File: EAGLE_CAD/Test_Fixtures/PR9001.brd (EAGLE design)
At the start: 62.5 x 47.5 mm, 14 parts, among them T10 PR9001_TESTPOINT, T11 PR9001_TESTPOINT, T12 PR9001_TESTPOINT, T13 PR9001_TESTPOINT, T2 PR9001_TESTPOINT, T3 PR9001_TESTPOINT, T4 PR9001_TESTPOINT, T5 PR9001_TESTPOINT

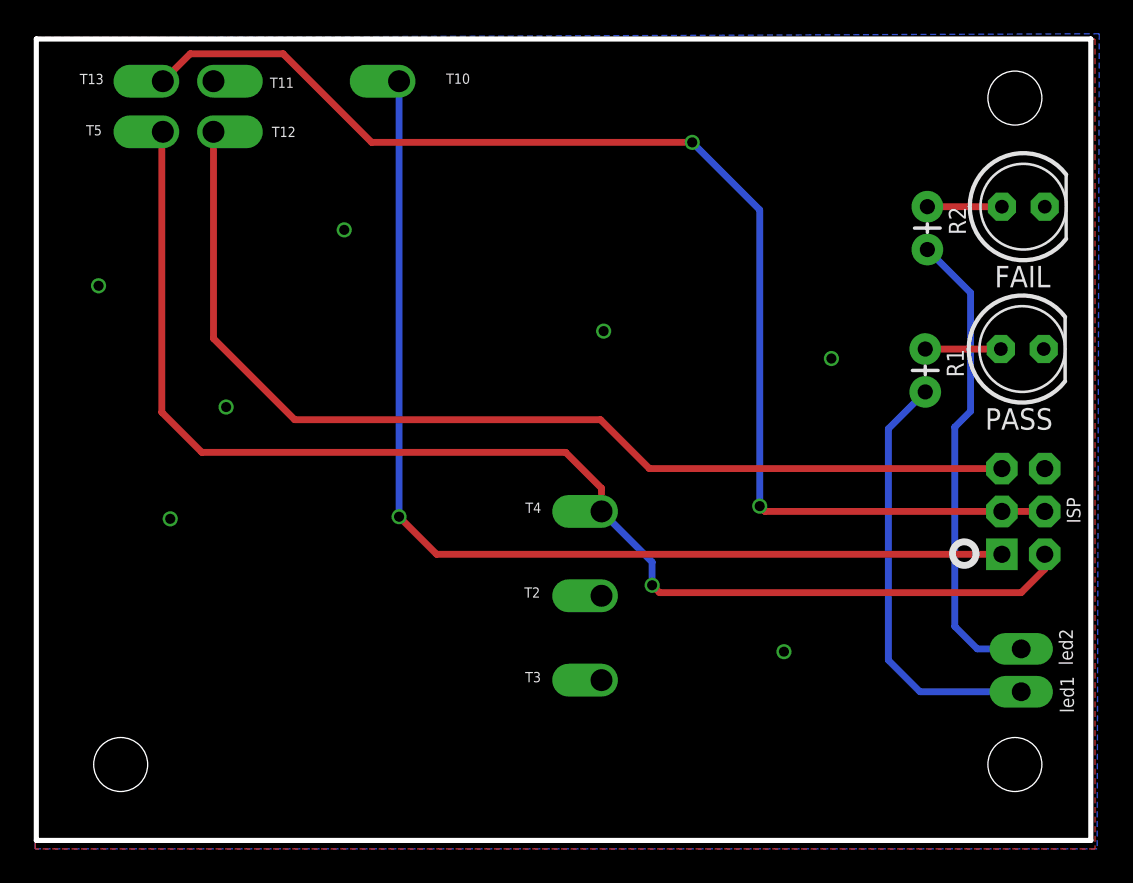
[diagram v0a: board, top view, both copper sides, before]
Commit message: PR9001 Programming Fixture
Updated layout and added an additional mounting hole.
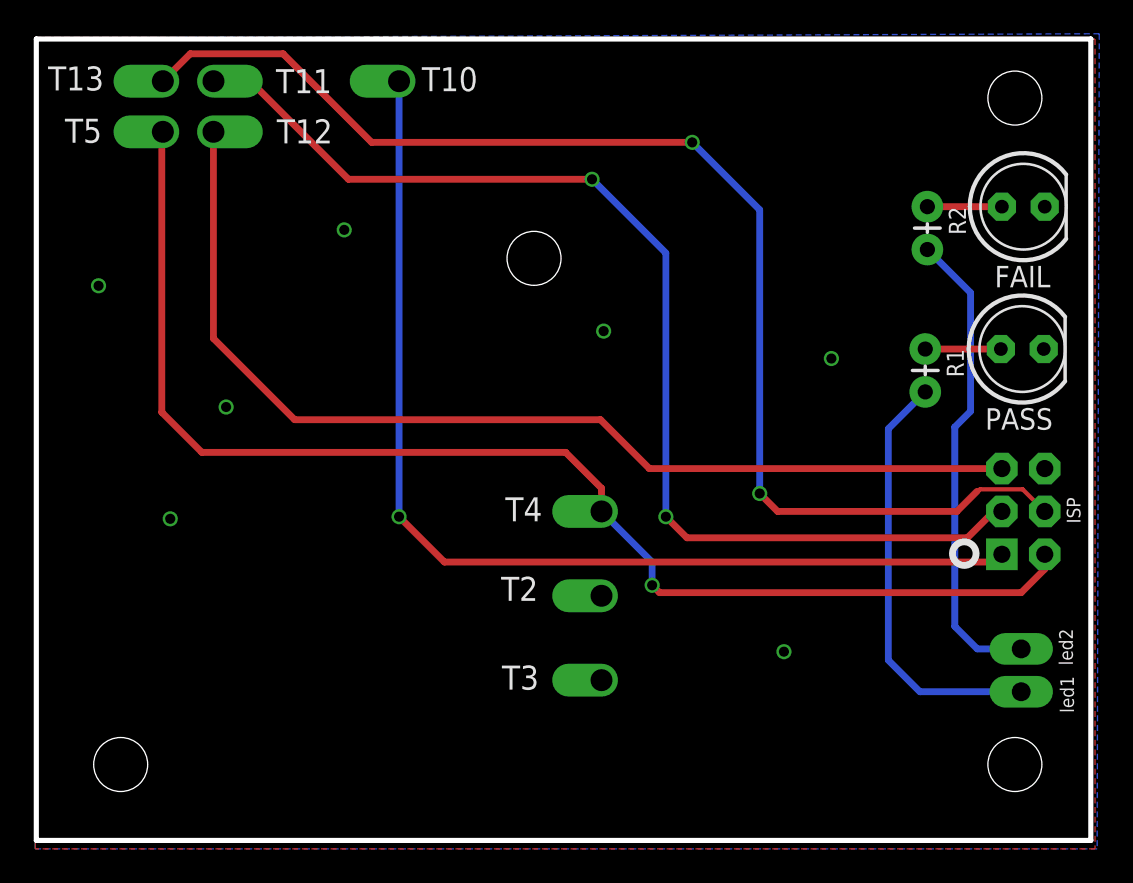
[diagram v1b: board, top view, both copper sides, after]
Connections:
- net SCLK: now also ISP.3
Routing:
- net SCLK: track 0.00 -> 67.7 mm, vias 0 -> 2
- net SDIO: track 74.5 -> 75.1 mm
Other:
- board text added: "PR9001 Fixture For Use With PR9024"
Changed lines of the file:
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@@
 <text x="87" y="28.0625" size="0.8128" layer="25" rot="R90">led1</text>
 <text x="86.9375" y="30.875" size="0.8128" layer="25" rot="R90">led2</text>
+<hole x="55" y="55" drill="3.2"/>
+<text x="61.6875" y="46.25" size="1.4224" layer="26" rot="MR0">PR9001 Fixture
+For Use With PR9024 </text>
 </plain>
 <attributes>
@@
 </element>
 <element name="T2" library="PR_Parts_Library" package="PR9001_TESTPOINT" value="PR9001_TESTPOINT" x="59" y="35" locked="yes" smashed="yes" rot="MR0">
-<attribute name="NAME" x="54.425" y="34.8876" size="0.6096" layer="25" font="vector" ratio="16"/>
+<attribute name="NAME" x="53.05" y="34.7001" size="1.4224" layer="25" font="vector" ratio="16"/>
 <attribute name="VALUE" x="59.508" y="34.238" size="0.254" layer="28" rot="MR0"/>
 </element>
 <element name="T3" library="PR_Parts_Library" package="PR9001_TESTPOINT" value="PR9001_TESTPOINT" x="59" y="30" locked="yes" smashed="yes" rot="MR0">
-<attribute name="NAME" x="54.475" y="29.8751" size="0.6096" layer="25" font="vector" ratio="16"/>
+<attribute name="NAME" x="53.1" y="29.4376" size="1.4224" layer="25" font="vector" ratio="16"/>
 <attribute name="VALUE" x="59.508" y="29.238" size="0.254" layer="28" rot="MR0"/>
 </element>
 <element name="T4" library="PR_Parts_Library" package="PR9001_TESTPOINT" value="PR9001_TESTPOINT" x="59" y="40" locked="yes" smashed="yes" rot="MR0">
-<attribute name="NAME" x="54.4875" y="39.9126" size="0.6096" layer="25" font="vector" ratio="16"/>
+<attribute name="NAME" x="53.3" y="39.4126" size="1.4224" layer="25" font="vector" ratio="16"/>
 <attribute name="VALUE" x="59.508" y="39.238" size="0.254" layer="28" rot="MR0"/>
 </element>
 <element name="T5" library="PR_Parts_Library" package="PR9001_TESTPOINT" value="PR9001_TESTPOINT" x="33" y="62.5" locked="yes" smashed="yes" rot="MR0">
-<attribute name="NAME" x="28.45" y="62.2876" size="0.6096" layer="25" font="vector" ratio="16"/>
+<attribute name="NAME" x="27.2" y="61.8501" size="1.4224" layer="25" font="vector" ratio="16"/>
 <attribute name="VALUE" x="33.508" y="61.738" size="0.254" layer="28" rot="MR0"/>
 </element>
 <element name="T10" library="PR_Parts_Library" package="PR9001_TESTPOINT" value="PR9001_TESTPOINT" x="47" y="65.5" locked="yes" smashed="yes" rot="MR0">
-<attribute name="NAME" x="49.79" y="65.3451" size="0.6096" layer="25" font="vector" ratio="16"/>
+<attribute name="NAME" x="48.3525" y="64.9076" size="1.4224" layer="25" font="vector" ratio="16"/>
 <attribute name="VALUE" x="47.508" y="64.738" size="0.254" layer="28" rot="MR0"/>
 </element>
 <element name="T11" library="PR_Parts_Library" package="PR9001_TESTPOINT" value="PR9001_TESTPOINT" x="36" y="65.5" locked="yes" smashed="yes" rot="MR180">
-<attribute name="NAME" x="40.7625" y="65.7124" size="0.6096" layer="25" font="vector" ratio="16" rot="R180"/>
+<attribute name="NAME" x="43.0125" y="66.2124" size="1.4224" layer="25" font="vector" ratio="16" rot="R180"/>
 <attribute name="VALUE" x="35.492" y="66.262" size="0.254" layer="28" rot="MR180"/>
 </element>
 <element name="T12" library="PR_Parts_Library" package="PR9001_TESTPOINT" value="PR9001_TESTPOINT" x="36" y="62.5" locked="yes" smashed="yes" rot="MR180">
-<attribute name="NAME" x="40.875" y="62.7999" size="0.6096" layer="25" font="vector" ratio="16" rot="R180"/>
+<attribute name="NAME" x="43.0625" y="63.2374" size="1.4224" layer="25" font="vector" ratio="16" rot="R180"/>
 <attribute name="VALUE" x="35.492" y="63.262" size="0.254" layer="28" rot="MR180"/>
 </element>
 <element name="T13" library="PR_Parts_Library" package="PR9001_TESTPOINT" value="PR9001_TESTPOINT" x="33" y="65.5" locked="yes" smashed="yes" rot="MR0">
-<attribute name="NAME" x="28.075" y="65.3251" size="0.6096" layer="25" font="vector" ratio="16"/>
+<attribute name="NAME" x="26.2" y="64.9501" size="1.4224" layer="25" font="vector" ratio="16"/>
 <attribute name="VALUE" x="33.508" y="64.738" size="0.254" layer="28" rot="MR0"/>
 </element>
@@
 <contactref element="ISP" pad="1"/>
 <contactref element="T10" pad="P$1"/>
-<wire x1="82.73" y1="37.46" x2="49.2275" y2="37.46" width="0.4064" layer="1"/>
-<wire x1="49.2275" y1="37.46" x2="47" y2="39.6875" width="0.4064" layer="1"/>
+<wire x1="49.6875" y1="37" x2="47" y2="39.6875" width="0.4064" layer="1"/>
 <via x="47" y="39.6875" extent="1-16" drill="0.6"/>
 <wire x1="47" y1="39.6875" x2="47" y2="65.5" width="0.4064" layer="16"/>
+<wire x1="49.6875" y1="37" x2="82.27" y2="37" width="0.4064" layer="1"/>
+<wire x1="82.27" y1="37" x2="82.73" y2="37.46" width="0.4064" layer="1"/>
 </signal>
 <signal name="SCLK">
 <contactref element="T11" pad="P$1"/>
+<contactref element="ISP" pad="3"/>
+<wire x1="82.73" y1="40" x2="82.25" y2="40" width="0.4064" layer="1"/>
+<wire x1="82.25" y1="40" x2="80.6875" y2="38.4375" width="0.4064" layer="1"/>
+<wire x1="80.6875" y1="38.4375" x2="64.0625" y2="38.4375" width="0.4064" layer="1"/>
+<via x="58.4375" y="59.6875" extent="1-16" drill="0.6"/>
+<wire x1="58.4375" y1="59.6875" x2="44" y2="59.6875" width="0.4064" layer="1"/>
+<wire x1="44" y1="59.6875" x2="38.1875" y2="65.5" width="0.4064" layer="1"/>
+<wire x1="38.1875" y1="65.5" x2="36" y2="65.5" width="0.4064" layer="1"/>
+<wire x1="64.0625" y1="38.4375" x2="62.8125" y2="39.6875" width="0.4064" layer="1"/>
+<via x="62.8125" y="39.6875" extent="1-16" drill="0.6"/>
+<wire x1="62.8125" y1="39.6875" x2="62.8125" y2="55.3125" width="0.4064" layer="16"/>
+<wire x1="62.8125" y1="55.3125" x2="58.4375" y2="59.6875" width="0.4064" layer="16"/>
 </signal>
 <signal name="SDIO">
 <contactref element="ISP" pad="4"/>
 <contactref element="T13" pad="P$1"/>
-<wire x1="85.27" y1="40" x2="68.6875" y2="40" width="0.4064" layer="1"/>
-<wire x1="68.6875" y1="40" x2="68.375" y2="40.3125" width="0.4064" layer="1"/>
-<via x="68.375" y="40.3125" extent="1-16" drill="0.6"/>
-<wire x1="68.375" y1="40.3125" x2="68.375" y2="57.875" width="0.4064" layer="16"/>
 <wire x1="68.375" y1="57.875" x2="64.375" y2="61.875" width="0.4064" layer="16"/>
 <via x="64.375" y="61.875" extent="1-16" drill="0.6"/>
@@
 <wire x1="40.125" y1="67.125" x2="34.625" y2="67.125" width="0.4064" layer="1"/>
 <wire x1="34.625" y1="67.125" x2="33" y2="65.5" width="0.4064" layer="1"/>
+<wire x1="80.0625" y1="40" x2="81.25" y2="41.1875" width="0.4064" layer="1"/>
+<wire x1="81.25" y1="41.1875" x2="81.3125" y2="41.1875" width="0.254" layer="1"/>
+<wire x1="81.3125" y1="41.1875" x2="81.4375" y2="41.3125" width="0.254" layer="1"/>
+<wire x1="81.4375" y1="41.3125" x2="83.9575" y2="41.3125" width="0.254" layer="1"/>
+<wire x1="83.9575" y1="41.3125" x2="85.27" y2="40" width="0.254" layer="1"/>
+<wire x1="80.0625" y1="40" x2="69.4375" y2="40" width="0.4064" layer="1"/>
+<wire x1="69.4375" y1="40" x2="68.375" y2="41.0625" width="0.4064" layer="1"/>
+<via x="68.375" y="41.0625" extent="1-16" drill="0.6"/>
+<wire x1="68.375" y1="41.0625" x2="68.375" y2="57.875" width="0.4064" layer="16"/>
 </signal>
 <signal name="VCC">
@@
 </board>
 </drawing>
+<compatibility>
+<note version="6.3" minversion="6.2.2" severity="warning">
+Since Version 6.2.2 text objects can contain more than one line,
+which will not be processed correctly with this version.
+</note>
+</compatibility>
 </eagle>
